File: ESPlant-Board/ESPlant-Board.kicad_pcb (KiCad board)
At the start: 4 copper layers, 24 x 46 mm, 38 parts, among them J1 Conn_01x05, U1 HC-TYPE-C-16P-01A-G, U13 ESP32-C6-MINI-1/U, U3 AHT20-F, U4 Button, U6 Light sensor, U7 AMS1117-3_3, U8 MK-12C02-G025

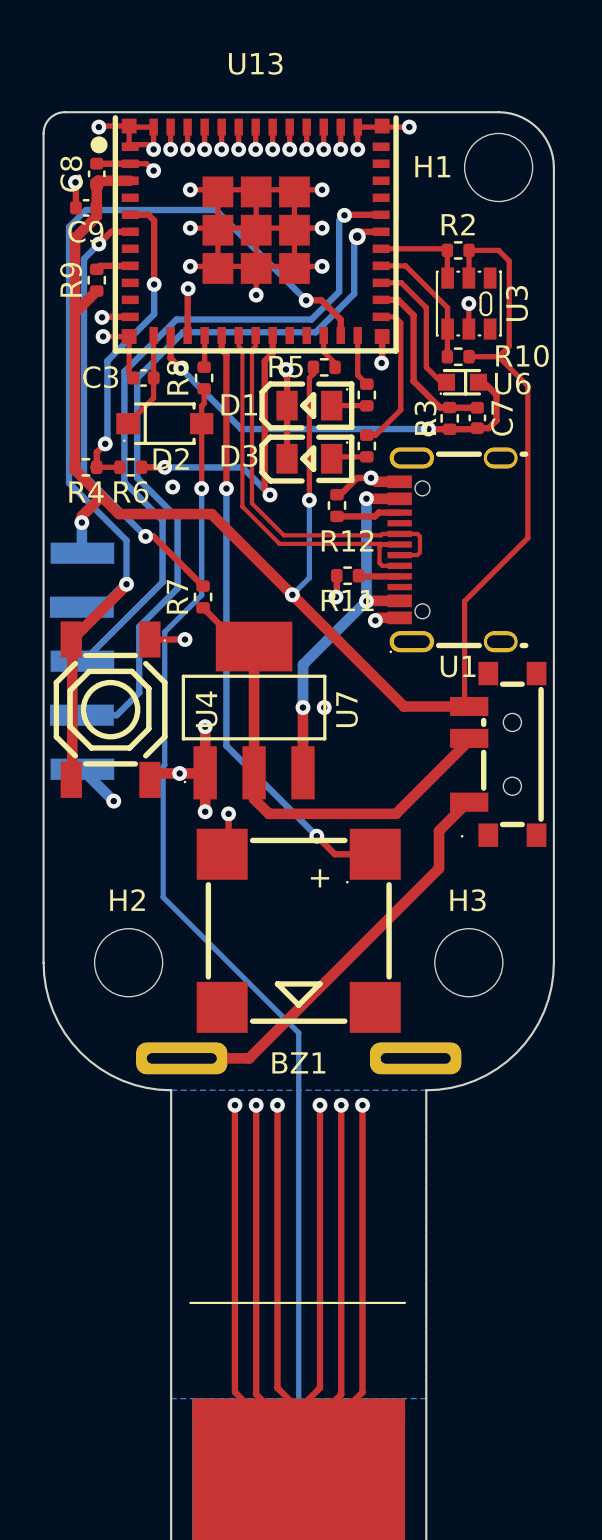
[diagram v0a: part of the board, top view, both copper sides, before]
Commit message: Board: New power supply chip
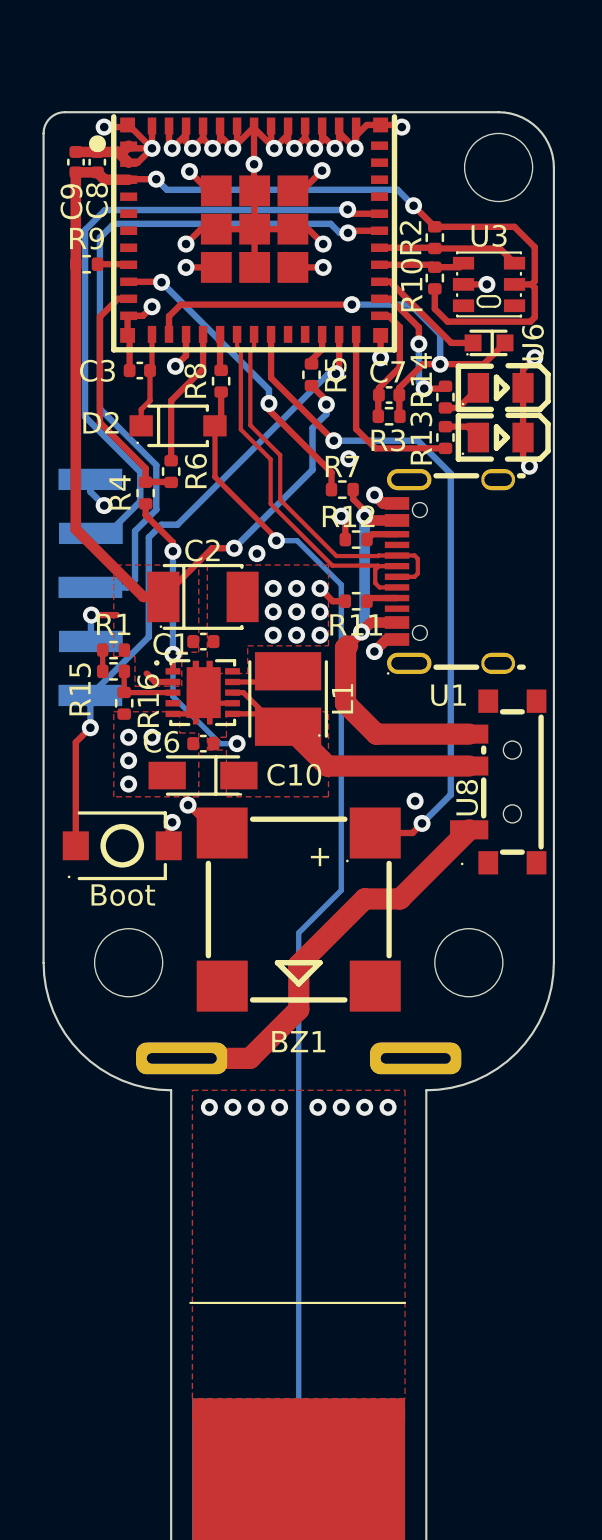
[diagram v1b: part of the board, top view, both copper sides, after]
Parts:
- removed U4: Button, CustomFootprints:SW-SMD_4P-L5.1-W5.1-P3.70-LS6.5-TL-2
- added C1: 2.2uF-Ceramic, Capacitor_SMD:C_0402_1005Metric, F.Cu at (160.5, 128.9)
- added C10: 10uF-Tantalum, CustomFootprints:CAP-SMD_L3.2-W1.6-RD-C7171, F.Cu at (160.5, 135.2)
- added C2: 100uF-Tantalum, CustomFootprints:CASE-B_3528, F.Cu at (160.5, 126.8)
- added C6: 100nF-Ceramic, Capacitor_SMD:C_0402_1005Metric, F.Cu at (160.5, 133.7)
- added L1: CD32YP0302-6R8M, CustomFootprints:IND-SMD_L3.5-W3.0, F.Cu at (164.5, 131.6)
- added R1: 100k, Resistor_SMD:R_0402_1005Metric, F.Cu at (156.3, 129.3)
- added R15: 1M, Resistor_SMD:R_0402_1005Metric, F.Cu at (156.3, 130.3)
- added R16: 200k, Resistor_SMD:R_0402_1005Metric, F.Cu at (156.8, 131.8)
- added U5: TPS61025DRCR, CustomFootprints:VSON-10_L3.0-W3.0-P0.50-BL-EP_TPS62410DRCR, F.Cu at (160.5, 131.3)
- U7: value AMS1117-3_3 -> TS-1088-AR02016; footprint CustomFootprints:SOT-223-3_L6.5-W3.4-P2.30-LS7.0-BR -> CustomFootprints:SW-SMD_L3.9-W3.0-P4.45
- moved U2 37.8 mm to (153.0, 111.7), turned to 0 degrees
- moved U10 37.7 mm to (177.0, 111.7), turned to 180 degrees
- moved U11 26.9 mm to (177.0, 139.7)
- moved U12 26.9 mm to (153.0, 139.7)
- moved D3 9.60 mm to (174.5, 117.0), turned to 180 degrees
- moved D1 9.12 mm to (174.5, 119.3), turned to 180 degrees
- moved U7 8.91 mm to (156.7, 138.5), turned to 180 degrees
- moved R7 8.27 mm to (167.1, 121.8), turned to 180 degrees
- moved R14 4.36 mm to (171.9, 117.4)
- moved C7 4.29 mm to (169.2, 117.3), turned to 180 degrees
- moved R13 4.21 mm to (171.9, 119.3), turned to 90 degrees
- moved J1 4.09 mm to (153.9, 126.3), turned to 180 degrees
- moved R10 3.86 mm to (171.4, 111.8), turned to -90 degrees
- moved R4 3.06 mm to (157.8, 121.9), turned to 90 degrees
- moved R3 2.85 mm to (169.2, 118.3), turned to 180 degrees
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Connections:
- J1 pad 2: /RX -> /TX
- J1 pad 3: /TX -> /RX
- J1 pad 4: /IO9 -> +3V3
- J1 pad 5: +3V3 -> /IO9
- R4 pad 1: +3V3 -> VCC
- R7 pad 2: Net-(U13-IO3) -> Net-(U13-IO4)
- U1 pad A4B9: Net-(U7-VIN) -> /USB
- U1 pad B4A9: Net-(U7-VIN) -> /USB
- U13 pad 10: unconnected-(U13-IO5-Pad10) -> /Voltage_Measurement_Analog
- U13 pad 15: /Square_Wave_Signal -> /Voltage_Measurement_Select
- U13 pad 16: /Buzzer -> /Square_Wave_Signal
- U13 pad 19: /Voltage_Measurement_Select -> /Buzzer
- U13 pad 25: /LED_RED -> /Light_Sensor_Select
- U13 pad 26: /Light_Sensor_Select -> /LED_RED
- U13 pad 5: /Voltage_Measurement_Analog -> unconnected-(U13-IO2-Pad5)
- U13 pad 6: Net-(U13-IO3) -> unconnected-(U13-IO3-Pad6)
- U13 pad 9: unconnected-(U13-IO4-Pad9) -> Net-(U13-IO4)
- U7 pad 2: /USB -> /IO9
- U8 pad 2: /USB -> VCC
- U8 pad 3: +3V3 -> /USB
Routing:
- net GND: track 182.8 -> 84.1 mm, vias 47 -> 55
- net VCC: track 0.00 -> 29.8 mm, vias 0 -> 3
- net Net-(U13-IO3): track 20.6 -> 0.00 mm, vias 2 -> 0
- net Net-(U7-VIN): track 17.3 -> 0.00 mm, vias 3 -> 0
- net /IO9: track 46.6 -> 30.0 mm
- net Net-(U13-IO4): track 0.00 -> 14.6 mm, vias 0 -> 2
- net +3V3: track 82.2 -> 73.3 mm, vias 3 -> 5
- net /Voltage_Measurement_Select: track 14.4 -> 6.56 mm, vias 2 -> 0
- net /LED_GREEN: track 2.57 -> 9.03 mm
- net /Voltage_Measurement_Analog: track 15.1 -> 11.6 mm, vias 2 -> 0
- net /FB: track 0.00 -> 3.29 mm
- net /Buzzer: track 28.6 -> 31.8 mm
- net /SW: track 0.00 -> 2.83 mm
- net /Light_Sensor_Select: track 8.44 -> 5.79 mm
- net /Light_Sensor_Analog: track 20.3 -> 23.0 mm
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- added copper zone on F.Cu, net +3V3
- added copper zone on F.Cu, net GND
- added copper zone on F.Cu, net VCC
- removed copper zone on B.Cu, net GND
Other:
- board text added: "Boot"

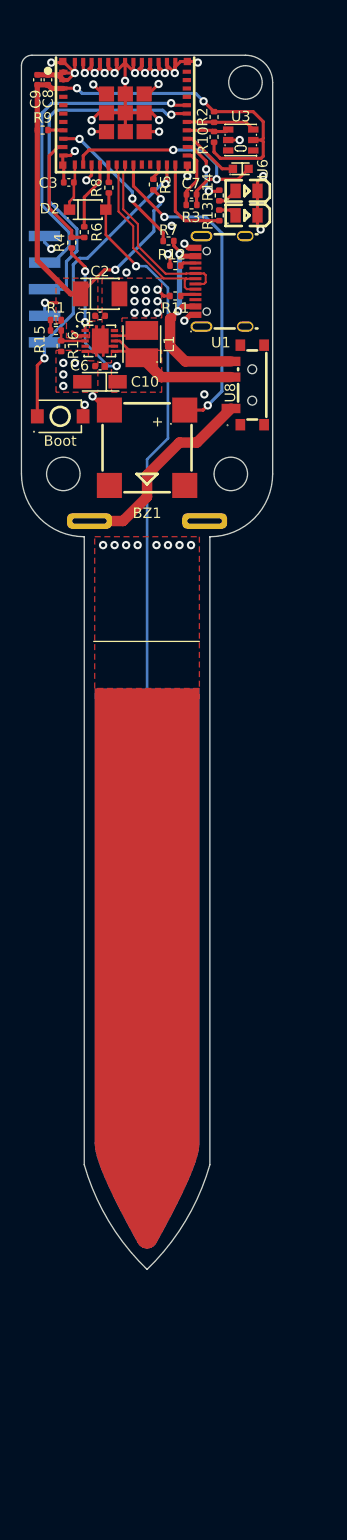
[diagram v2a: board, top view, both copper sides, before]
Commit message: Board: Update Layout
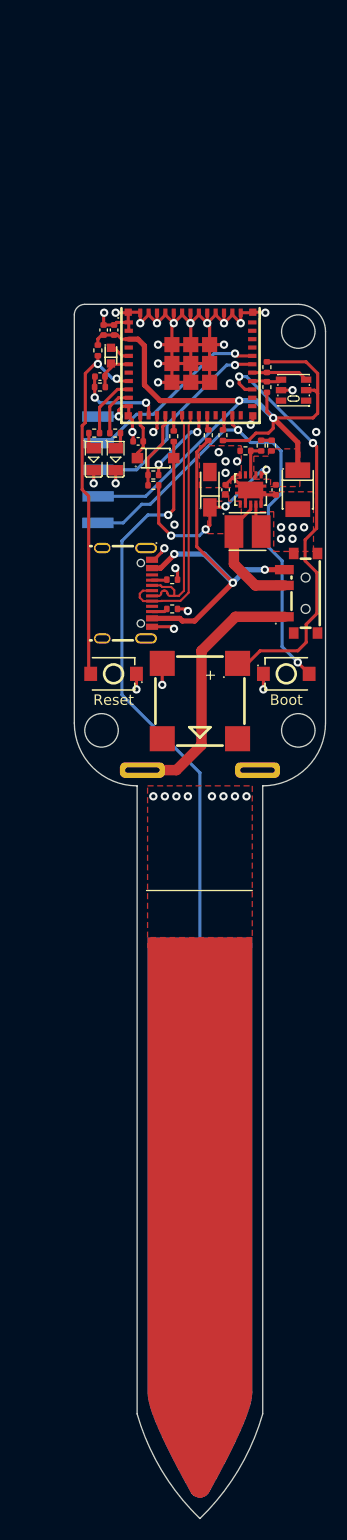
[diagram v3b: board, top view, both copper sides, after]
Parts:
- added U4: Tactile-Switch, CustomFootprints:SW-SMD_L3.9-W3.0-P4.45, F.Cu at (161.8, 163.1)
- D2: value SOD-123-Switching-Diode -> Switching-Diode
- L1: value CD32YP0302-6R8M -> 6.8uH
- U1: value HC-TYPE-C-16P-01A-G -> USB-C
- U13: value ESP32-C6-MINI-1/U -> ESP32-C6-MINI-1-N4
- U5: value TPS61025DRCR -> 3.3V-Regulator
- U7: value TS-1088-AR02016 -> Tactile-Switch
- U8: value MK-12C02-G025 -> Slide-Switch
- U9: value ~ -> Battery-Spring
- moved R12 32.8 mm to (167.4, 156.9), turned to 180 degrees
- moved U7 32.7 mm to (178.3, 163.1), turned to 0 degrees
- moved U1 31.1 mm to (163.1, 155.4), turned to -90 degrees
- moved D3 29.5 mm to (159.9, 142.6), turned to 90 degrees
- moved R11 27.1 mm to (167.4, 154.1), turned to 180 degrees
- moved C2 26.6 mm to (179.4, 145.5), turned to -90 degrees
- moved D1 26.4 mm to (162.0, 142.6), turned to 90 degrees
- moved R14 25.7 mm to (159.9, 140.1), turned to 180 degrees
- moved C3 25.6 mm to (164.1, 140.9)
- moved H3 25.3 mm to (179.4, 168.5)
- moved R5 24.9 mm to (172.2, 140.3)
- moved H2 24.8 mm to (160.6, 168.5)
- moved U13 24.8 mm to (169.1, 133.5)
- moved C8 24.7 mm to (161.8, 130.2)
- moved C9 24.7 mm to (160.8, 130.2)
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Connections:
- net /AD_Capacitance renamed ADC_Moisture
- net /BAT renamed PWR_BAT_VIN
- net /D+ renamed USB_D+
- net /D- renamed USB_D-
- net /EN renamed EN
- net /FB renamed PWR_FB
- net /IO8 renamed IO8
- net /IO9 renamed IO9
- net /RX renamed RX
- net /SensorCapV renamed Moisture_SensorCapV
- net /Square_Wave_Signal renamed Moisture_Square_Wave_Signal
- net /TH_SCL renamed TH_SCL
- net /TH_SDA renamed TH_SDA
- net /TX renamed TX
- net /USB renamed PWR_USB_VIN
- net Net-(U1-CC1) renamed PWR_USB_CC1
- net Net-(U1-CC2) renamed PWR_USB_CC2
- BZ1 pad 1: /Buzzer -> Buzzer
- BZ1 pad 3: (no net) -> unconnected-(BZ1-NC-Pad3)
- BZ1 pad 4: (no net) -> unconnected-(BZ1-NC-Pad4)
- C10 pad 1: VCC -> PWR_VIN
- C6 pad 1: VCC -> PWR_VIN
- C7 pad 1: /Light_Sensor_Analog -> ADC_Light_Sensor
- C7 pad 2: /Light_Sensor_Select -> Light_Sensor_Select
- L1 pad 1: /SW -> PWR_VIN
- L1 pad 2: VCC -> PWR_SW
- R13 pad 1: /LED_GREEN -> LED_Green
- R14 pad 1: /LED_RED -> LED_Red
- R3 pad 1: /Light_Sensor_Analog -> ADC_Light_Sensor
- R3 pad 2: /Light_Sensor_Select -> Light_Sensor_Select
- R4 pad 1: VCC -> PWR_VIN
- R4 pad 2: /Voltage_Measurement_Analog -> ADC_Voltage_Measurement
- R6 pad 1: /Voltage_Measurement_Analog -> ADC_Voltage_Measurement
- R6 pad 2: /Voltage_Measurement_Select -> Voltage_Measurement_Select
- R7 pad 2: Net-(U13-IO4) -> Net-(U13-IO15)
- U13 pad 10: /Voltage_Measurement_Analog -> LED_Green
- U13 pad 13: /Light_Sensor_Analog -> Light_Sensor_Select
- U13 pad 15: /Voltage_Measurement_Select -> ADC_Voltage_Measurement
- U13 pad 19: /Buzzer -> Voltage_Measurement_Select
- U13 pad 20: unconnected-(U13-IO15-Pad20) -> Net-(U13-IO15)
- U13 pad 24: /LED_GREEN -> unconnected-(U13-IO18-Pad24)
- U13 pad 25: /Light_Sensor_Select -> unconnected-(U13-IO19-Pad25)
- U13 pad 26: /LED_RED -> unconnected-(U13-IO20-Pad26)
- U13 pad 27: /Light_Sensor_In -> Buzzer
- U13 pad 5: unconnected-(U13-IO2-Pad5) -> Light_Sensor_In
- U13 pad 6: unconnected-(U13-IO3-Pad6) -> ADC_Light_Sensor
- U13 pad 9: Net-(U13-IO4) -> LED_Red
- U5 pad 1: VCC -> PWR_VIN
- U5 pad 6: VCC -> PWR_VIN
- U5 pad 8: VCC -> PWR_VIN
- U5 pad 9: /SW -> PWR_SW
- U6 pad 1: /Light_Sensor_In -> Light_Sensor_In
- U6 pad 2: /Light_Sensor_Analog -> ADC_Light_Sensor
- U8 pad 2: VCC -> PWR_VIN
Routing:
- net Buzzer: track 0.00 -> 39.8 mm, vias 0 -> 2
- net EN: track 1.48 -> 35.1 mm, vias 0 -> 2
- net /Buzzer: track 31.8 -> 0.00 mm, vias 2 -> 0
- net PWR_VIN: track 0.00 -> 30.8 mm, vias 0 -> 4
- net VCC: track 29.8 -> 0.00 mm, vias 3 -> 0
- net /Light_Sensor_Analog: track 23.0 -> 0.00 mm, vias 2 -> 0
- net PWR_USB_VIN: track 20.5 -> 39.7 mm, vias 2 -> 3
- net GND: track 84.1 -> 101.1 mm, vias 55 -> 48
- net IO9: track 30.0 -> 47.0 mm
- net Net-(U13-IO4): track 14.6 -> 0.00 mm, vias 2 -> 0
- net RX: track 33.5 -> 19.7 mm
- net TX: track 31.1 -> 18.4 mm
- net /Voltage_Measurement_Analog: track 11.6 -> 0.00 mm
- net /LED_GREEN: track 9.03 -> 0.00 mm
- net Light_Sensor_Select: track 0.00 -> 8.43 mm, vias 0 -> 2
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- added copper zone on F.Cu, net PWR_VIN
- removed copper zone on F.Cu, net VCC
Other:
- board text added: "Reset"
- board text added: "USB〡BAT"

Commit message: Panel: Update production files
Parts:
- moved R14 5.85 mm to (160.7, 145.9)
- moved R13 5.85 mm to (162.7, 145.9)
- moved D3 5.76 mm to (160.7, 148.3)
- moved D1 5.75 mm to (162.7, 148.3)
- moved U10 0.10 mm to (182.1, 135.3)
- moved U12 0.10 mm to (157.9, 163.5)
- moved U2 0.10 mm to (157.9, 135.3)
- moved U11 0.10 mm to (182.1, 163.5)
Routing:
- net GND: track 101.1 -> 214.8 mm, vias 48 -> 47
- net LED_Green: track 4.70 -> 10.9 mm
- net LED_Red: track 5.96 -> 12.0 mm

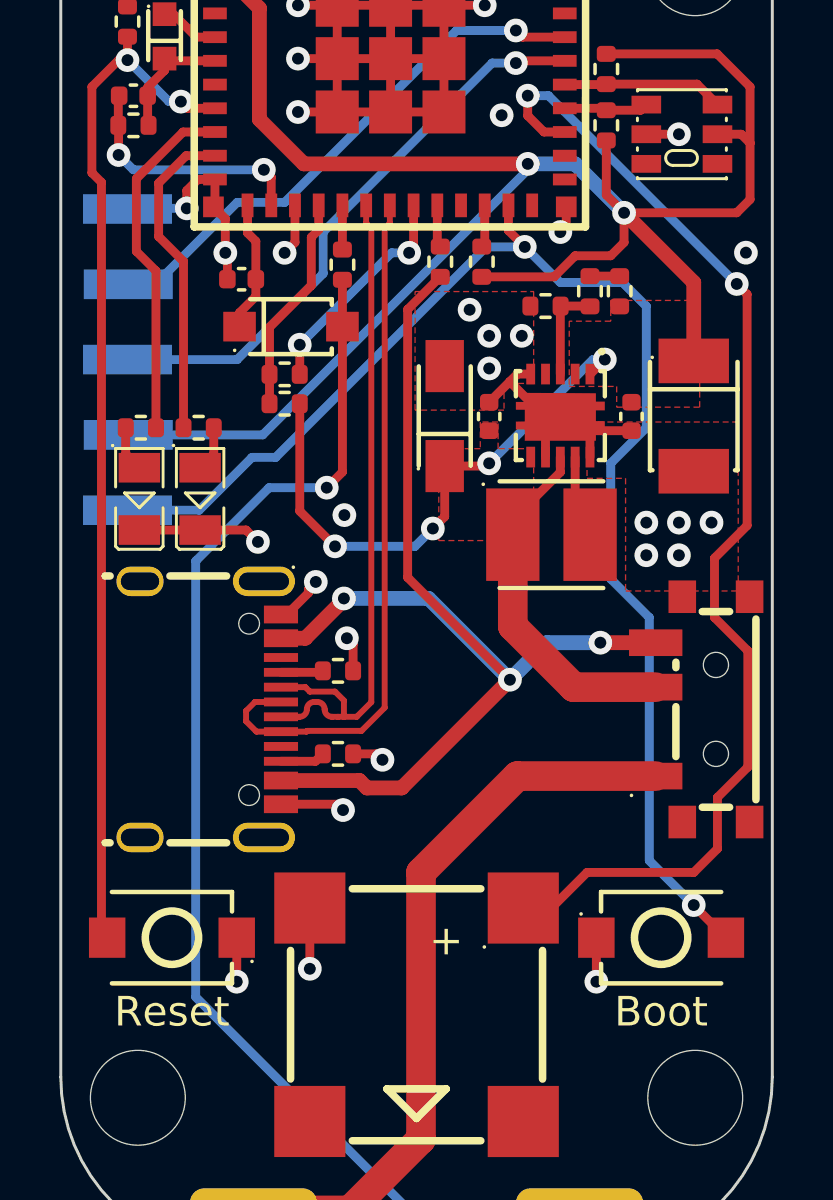
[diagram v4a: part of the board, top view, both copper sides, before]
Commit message: Board: Add debouncing caps to buttons
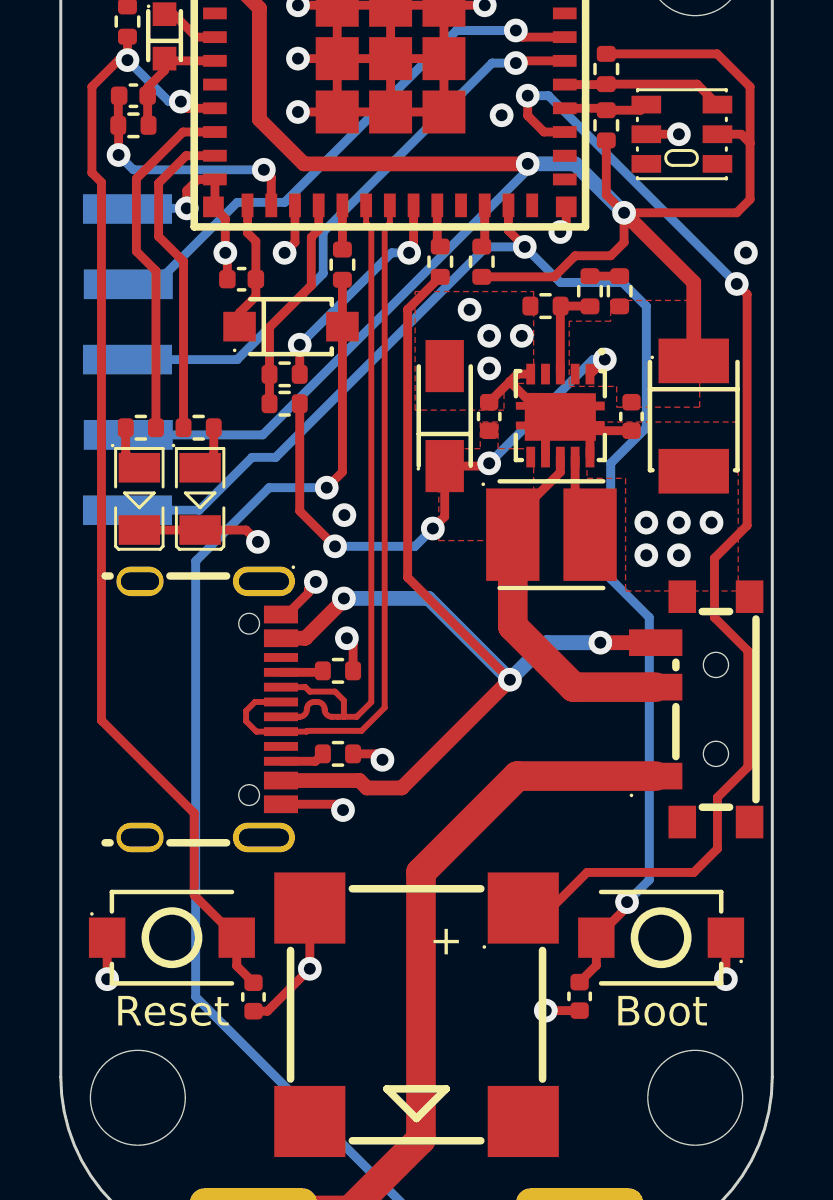
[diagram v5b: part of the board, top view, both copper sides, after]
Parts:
- added C11: 100nF-Ceramic, Capacitor_SMD:C_0402_1005Metric, F.Cu at (164.5, 165.1)
- added C5: 100nF-Ceramic, Capacitor_SMD:C_0402_1005Metric, F.Cu at (175.5, 165.1)
- turned U4 to 0 degrees
- turned U7 to 180 degrees
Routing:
- net GND: track 214.8 -> 218.5 mm, vias 47 -> 48
- net EN: track 34.9 -> 38.5 mm
- net IO9: track 47.0 -> 48.4 mm
